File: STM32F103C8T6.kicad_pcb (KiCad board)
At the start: 2 copper layers, 39.4 x 64.8 mm, 51 parts, among them J1 USB_Device, J2 USB_TTL, P1 L-Pin, P2 R-Pin, P3 DEBUG, SW1 NRST, U1 MIC5219-3.3YM5, U2 CH340E, U3 STM32F103C8Tx, Y1 8MHz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

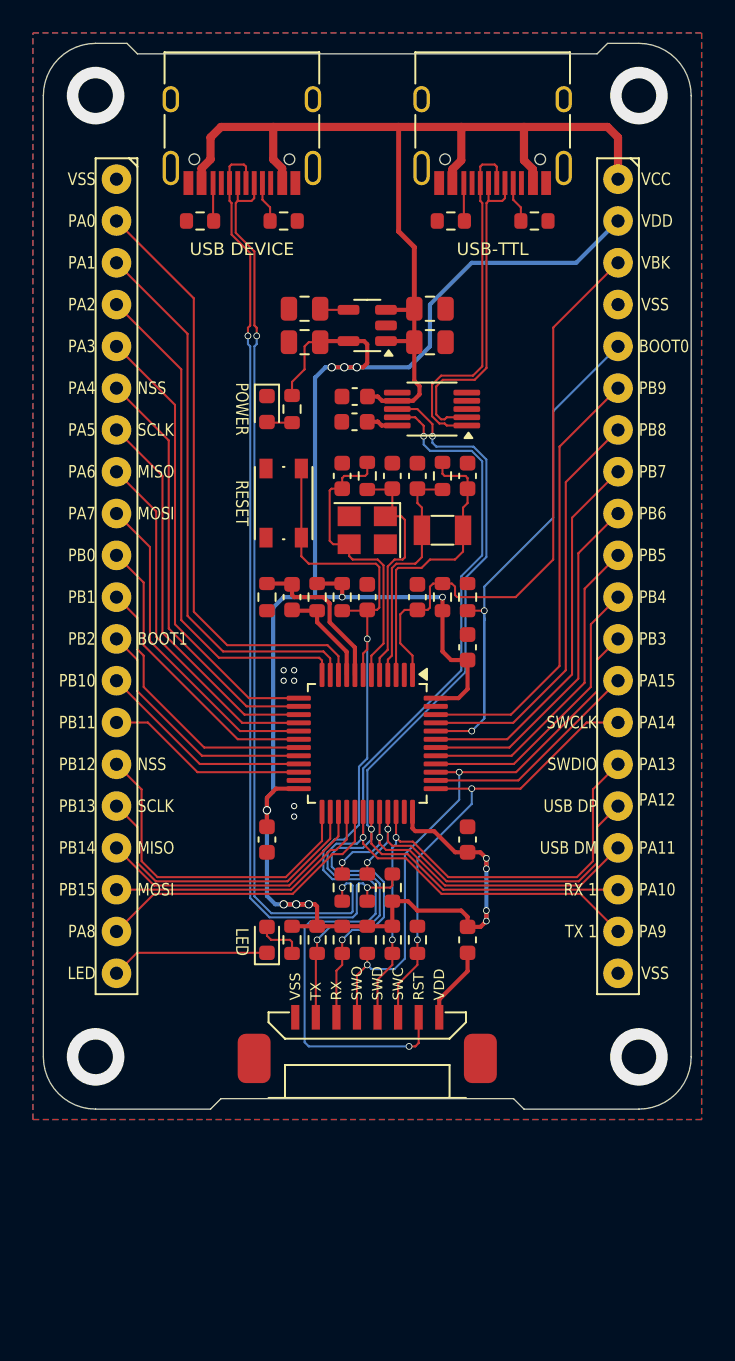
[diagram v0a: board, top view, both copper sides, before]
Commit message: 增加独立的电源连接端子
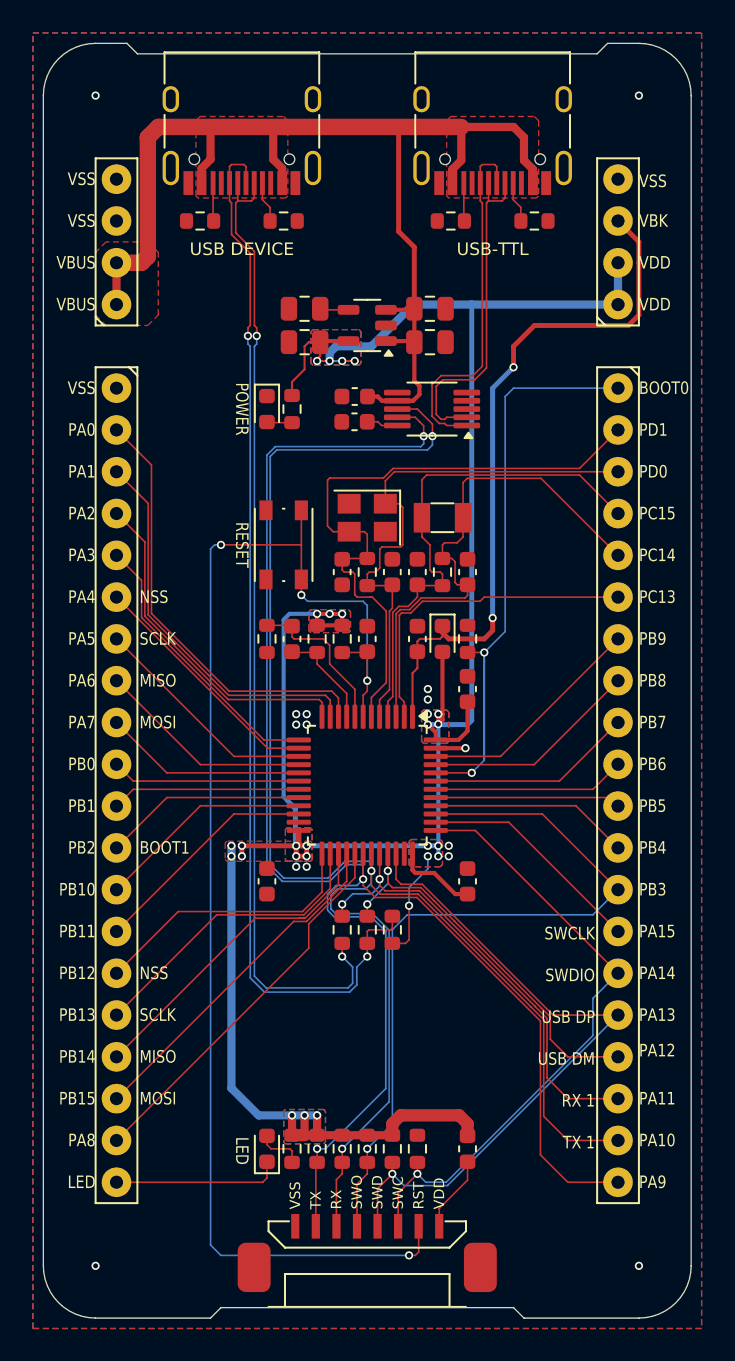
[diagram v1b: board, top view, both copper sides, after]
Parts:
- removed R15: 0R, Resistor_SMD:R_0603_1608Metric
- added D3: 1N4148, Diode_SMD:D_0603_1608Metric, F.Cu at (154.6, 115.6)
- added P4: POWER-R, Append_Connector:HDR1×4_2.54mm, F.Cu at (165.2, 95.2)
- added P5: POWER-L, Append_Connector:HDR1×4_2.54mm, F.Cu at (134.8, 95.2)
- moved D2 12.7 mm to (143.9, 146.5)
- moved F1 12.7 mm to (156.1, 146.5)
- moved P1 12.7 mm to (134.8, 100.3)
- moved P2 12.7 mm to (165.2, 100.3)
- moved P3 12.7 mm to (150.0, 151.8)
- moved R17 12.7 mm to (147.0, 146.5)
- moved R18 12.7 mm to (148.5, 146.5)
- moved R19 12.7 mm to (150.0, 146.5)
- moved R20 12.7 mm to (151.5, 146.5)
- moved R21 12.7 mm to (153.0, 146.5)
- moved R7 12.7 mm to (145.4, 146.5)
- moved C10 5.84 mm to (153.0, 111.5)
- moved C7 5.84 mm to (151.5, 111.5)
- moved C8 5.84 mm to (148.5, 111.5), turned to -90 degrees
- moved C9 5.84 mm to (156.1, 111.5)
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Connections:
- P2 pad 1: VBUS -> /BOOT0
- P2 pad 10: /PB5 -> /PB6
- P2 pad 11: /PB4 -> /PB5
- P2 pad 12: /PB3/SWO -> /PB4
- P2 pad 13: /PA15 -> /PB3/SWO
- P2 pad 14: /PA14/SWCLK -> /PA15
- P2 pad 15: /PA13/SWDIO -> /PA14/SWCLK
- P2 pad 16: /PA12/USBDP -> /PA13/SWDIO
- P2 pad 17: /PA11/USBDM -> /PA12/USBDP
- P2 pad 18: /PA10/USART_RX -> /PA11/USBDM
- P2 pad 19: /PA9/USART_TX -> /PA10/USART_RX
- P2 pad 2: VDD -> /PD1/OSC_OUT
- P2 pad 20: VSS -> /PA9/USART_TX
- P2 pad 3: VBAT -> /PD0/OSC_IN
- P2 pad 4: VSS -> /PC15/OSC32_OUT
- P2 pad 5: /BOOT0 -> /PC14/OSC32_IN
- P2 pad 6: /PB9 -> /PC13
- P2 pad 7: /PB8 -> /PB9
- P2 pad 8: /PB7 -> /PB8
- P2 pad 9: /PB6 -> /PB7
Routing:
- net VDD: track 124.8 -> 164.1 mm, vias 13 -> 27
- net /PA10/USART_RX: track 68.8 -> 100.7 mm
- net /PA9/USART_TX: track 70.6 -> 102.4 mm
- net VBUS: track 65.5 -> 87.5 mm
- net /NRST: track 60.3 -> 82.1 mm, vias 2 -> 4
- net /PD1/OSC_OUT: track 18.1 -> 39.2 mm
- net /PC13: track 0.00 -> 20.0 mm
- net /PD0/OSC_IN: track 15.0 -> 33.3 mm
- net /PC15/OSC32_OUT: track 14.5 -> 30.9 mm
- net /PC14/OSC32_IN: track 17.8 -> 31.7 mm
- net /PB9: track 27.1 -> 14.0 mm
- net /PB8: track 25.1 -> 13.2 mm
- net /PB3/SWO: track 35.0 -> 46.6 mm, vias 2 -> 1
- net /PA4: track 25.8 -> 14.9 mm
- net /PB7: track 23.4 -> 12.6 mm
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- added copper zone on F.Cu, net VBUS
- added copper zone on B.Cu, net VDD
- added copper zone on F.Cu, net VDD
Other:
- board size 39.4 x 64.8 mm -> 39.4 x 77.5 mm
- board text added: "PC13"
- board text added: "PC14"
- board text added: "PC15"
- board text added: "PD0"
- board text added: "PD1"
- board text added: "VBUS"
- board text removed: "VCC"

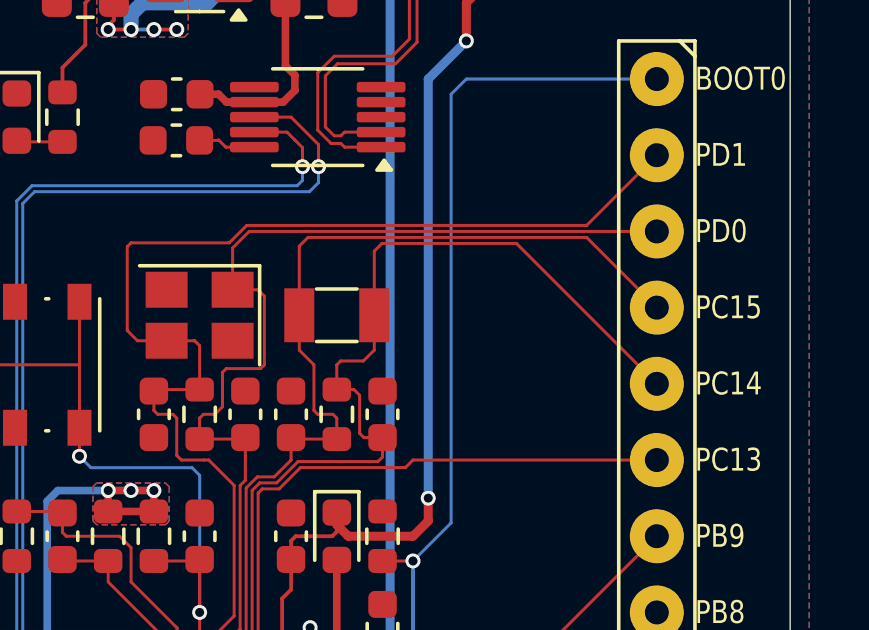
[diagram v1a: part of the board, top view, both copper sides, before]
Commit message: 修正晶振匹配电容铺地连接错误的问题
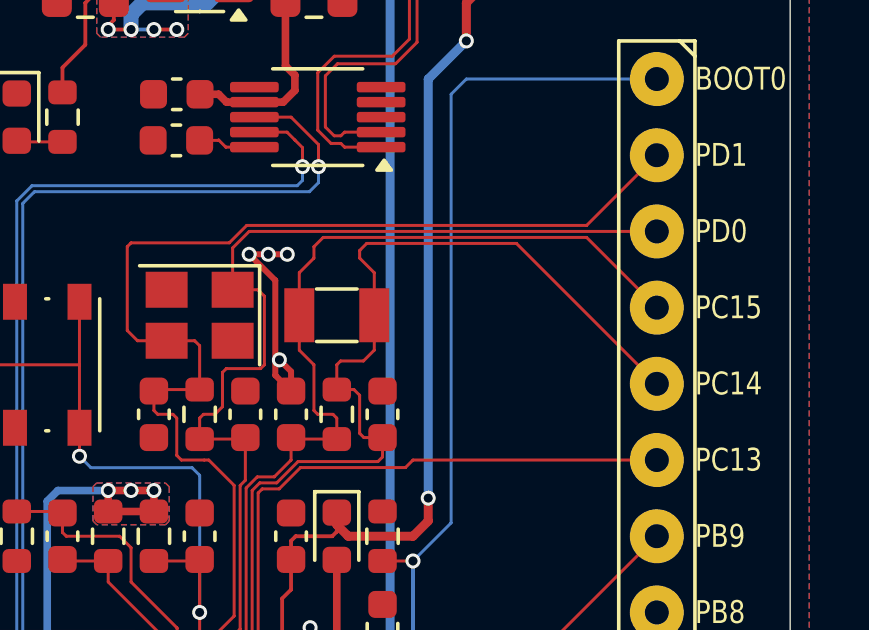
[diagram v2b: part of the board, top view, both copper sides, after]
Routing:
- net VSS: track 1.81 -> 9.42 mm, vias 11 -> 15
- net /PC14/OSC32_IN: track 31.7 -> 32.4 mm
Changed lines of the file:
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@@
 		)
 		(property "Value" "22pF"
-			(at -0.1524 0 360)
+			(at -0.1524 0 0)
 			(layer "F.Fab")
 			(effects
@@
 	)
 	(segment
+		(start 152.522 107.033)
+		(end 151.651 106.162)
+		(width 0.2)
+		(layer "F.Cu")
+		(net 1)
+	)
+	(segment
+		(start 153.048 110.721)
+		(end 153.048 110.068883)
+		(width 0.2)
+		(layer "F.Cu")
+		(net 1)
+	)
+	(segment
+		(start 153.048 110.721)
+		(end 152.522 110.195)
+		(width 0.2)
+		(layer "F.Cu")
+		(net 1)
+	)
+	(segment
+		(start 151.651 106.162)
+		(end 152.286 106.162)
+		(width 0.2)
+		(layer "F.Cu")
+		(net 1)
+	)
+	(segment
+		(start 153.048 110.068883)
+		(end 152.659 109.679883)
+		(width 0.2)
+		(layer "F.Cu")
+		(net 1)
+	)
+	(segment
 		(start 154.1625 122.2)
 		(end 155.969 122.2)
@@
 		(net 1)
 	)
+	(segment
+		(start 152.286 106.162)
+		(end 152.921 106.162)
+		(width 0.2)
+		(layer "F.Cu")
+		(net 1)
+	)
+	(segment
+		(start 152.522 110.195)
+		(end 152.522 107.033)
+		(width 0.2)
+		(layer "F.Cu")
+		(net 1)
+	)
+	(via
+		(at 151.651 106.162)
+		(size 0.5)
+		(drill 0.3)
+		(layers "F.Cu" "B.Cu")
+		(net 1)
+	)
 	(via
 		(at 153.683 119.243)
@@
 	)
 	(via
+		(at 152.659 109.679883)
+		(size 0.5)
+		(drill 0.3)
+		(layers "F.Cu" "B.Cu")
+		(net 1)
+	)
+	(via
+		(at 152.286 106.162)
+		(size 0.5)
+		(drill 0.3)
+		(layers "F.Cu" "B.Cu")
+		(net 1)
+	)
+	(via
+		(at 152.921 106.162)
+		(size 0.5)
+		(drill 0.3)
+		(layers "F.Cu" "B.Cu")
+		(net 1)
+	)
+	(via
 		(at 154.953 128.133)
 		(size 0.5)
@@
 	)
 	(segment
-		(start 153.280042 113.0708)
-		(end 155.9436 113.0708)
+		(start 155.822 106.777)
+		(end 155.822 108.194)
 		(width 0.1)
 		(layer "F.Cu")
@@
 	)
 	(segment
-		(start 155.822 106.055)
-		(end 155.822 108.194)
+		(start 153.280042 113.0708)
+		(end 155.9436 113.0708)
 		(width 0.1)
 		(layer "F.Cu")
@@
 	)
 	(segment
-		(start 160.56 105.8)
-		(end 156.077 105.8)
-		(width 0.1)
-		(layer "F.Cu")
-		(net 7)
-	)
-	(segment
-		(start 165.24 110.48)
-		(end 160.56 105.8)
-		(width 0.1)
-		(layer "F.Cu")
-		(net 7)
-	)
-	(segment
 		(start 155.474 112.271)
 		(end 155.334 112.131)
@@
 	)
 	(segment
+		(start 155.334 106.289)
+		(end 155.822 106.777)
+		(width 0.1)
+		(layer "F.Cu")
+		(net 7)
+	)
+	(segment
 		(start 156.096 112.271)
 		(end 155.474 112.271)
@@
 	)
 	(segment
+		(start 155.569 105.8)
+		(end 155.334 106.035)
+		(width 0.1)
+		(layer "F.Cu")
+		(net 7)
+	)
+	(segment
 		(start 152.568842 113.782)
 		(end 153.280042 113.0708)
@@
 	)
 	(segment
+		(start 165.24 110.48)
+		(end 160.56 105.8)
+		(width 0.1)
+		(layer "F.Cu")
+		(net 7)
+	)
+	(segment
+		(start 160.56 105.8)
+		(end 155.569 105.8)
+		(width 0.1)
+		(layer "F.Cu")
+		(net 7)
+	)
+	(segment
 		(start 154.572 109.845)
 		(end 154.572 110.671)
@@
 	)
 	(segment
-		(start 156.077 105.8)
-		(end 155.822 106.055)
+		(start 155.334 106.035)
+		(end 155.334 106.289)
 		(width 0.1)
 		(layer "F.Cu")
@@
 	)
 	(segment
-		(start 153.322 105.888)
-		(end 153.61 105.6)
-		(width 0.1)
-		(layer "F.Cu")
-		(net 8)
-	)
-	(segment
 		(start 153.322 108.194)
 		(end 153.322 109.357)
@@
 	)
 	(segment
+		(start 162.9 105.6)
+		(end 154.118 105.6)
+		(width 0.1)
+		(layer "F.Cu")
+		(net 8)
+	)
+	(segment
 		(start 153.937 111.496)
 		(end 154.445 111.496)
@@
 	)
 	(segment
+		(start 153.81 105.908)
+		(end 153.81 106.289)
+		(width 0.1)
+		(layer "F.Cu")
+		(net 8)
+	)
+	(segment
 		(start 153.098 112.321)
 		(end 153.048 112.271)
@@
 	)
 	(segment
-		(start 153.322 108.194)
-		(end 153.322 105.888)
-		(width 0.1)
-		(layer "F.Cu")
-		(net 8)
-	)
-	(segment
 		(start 153.322 109.357)
 		(end 153.81 109.845)
@@
 	)
 	(segment
-		(start 151.920315 113.582)
-		(end 152.486 113.582)
+		(start 153.322 106.777)
+		(end 153.322 108.194)
 		(width 0.1)
 		(layer "F.Cu")
@@
 	)
 	(segment
-		(start 162.9 105.6)
-		(end 165.24 107.94)
+		(start 151.920315 113.582)
+		(end 152.486 113.582)
 		(width 0.1)
 		(layer "F.Cu")
@@
 	)
 	(segment
-		(start 151.55 119.062)
-		(end 151.55 113.952315)
+		(start 154.118 105.6)
+		(end 153.81 105.908)
+		(width 0.1)
+		(layer "F.Cu")
+		(net 8)
+	)
+	(segment
+		(start 153.81 106.289)
+		(end 153.322 106.777)
 		(width 0.1)
 		(layer "F.Cu")
@@
 	)
 	(segment
-		(start 153.61 105.6)
+		(start 165.24 107.94)
 		(end 162.9 105.6)
 		(width 0.1)
 		(layer "F.Cu")
+		(net 8)
+	)
+	(segment
+		(start 151.55 119.062)
+		(end 151.55 113.952315)
+		(width 0.1)
+		(layer "F.Cu")

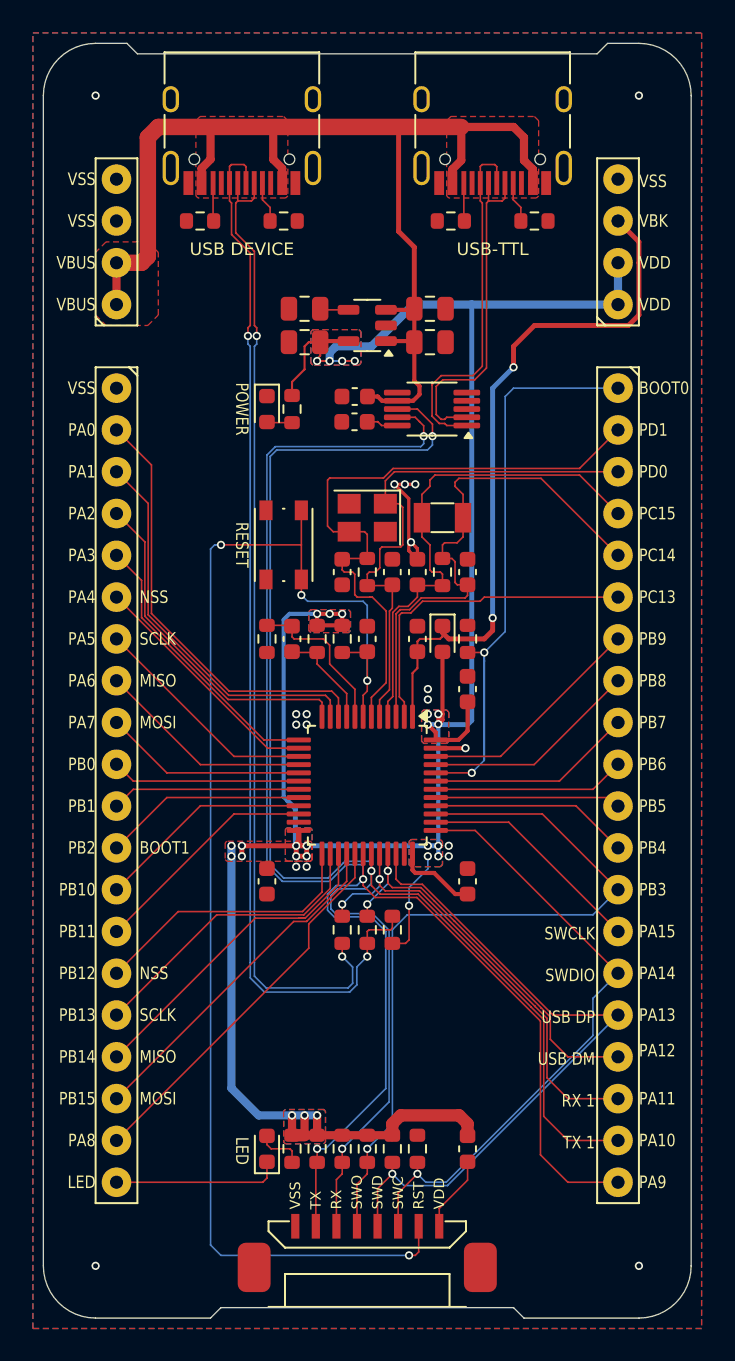
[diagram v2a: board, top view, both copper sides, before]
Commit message: 修正电器规则和布线错误
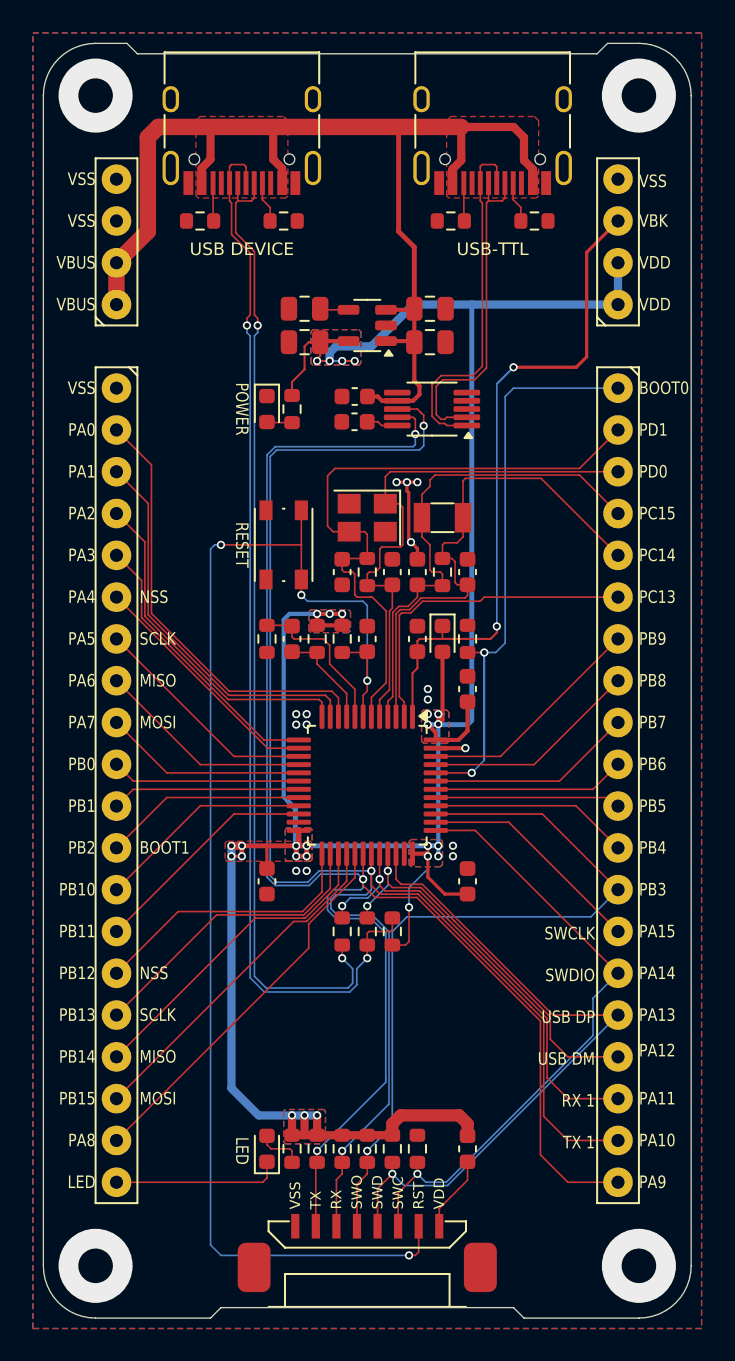
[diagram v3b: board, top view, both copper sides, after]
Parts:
- moved R3 0.10 mm to (151.5, 133.3)
- moved R4 0.10 mm to (148.5, 133.3)
- moved R5 0.10 mm to (150.0, 133.3)
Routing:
- net VDD: track 164.1 -> 167.6 mm
- net VBAT: track 43.3 -> 40.8 mm
- net VSS: track 9.42 -> 8.03 mm
- net /PA9/USART_TX: track 102.4 -> 101.3 mm
- net VBUS: track 87.5 -> 86.6 mm
- net /PC14/OSC32_IN: track 32.4 -> 31.7 mm
- net /PA10/USART_RX: track 100.7 -> 100.1 mm

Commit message: 更新电路设计，兼容F401CC芯片
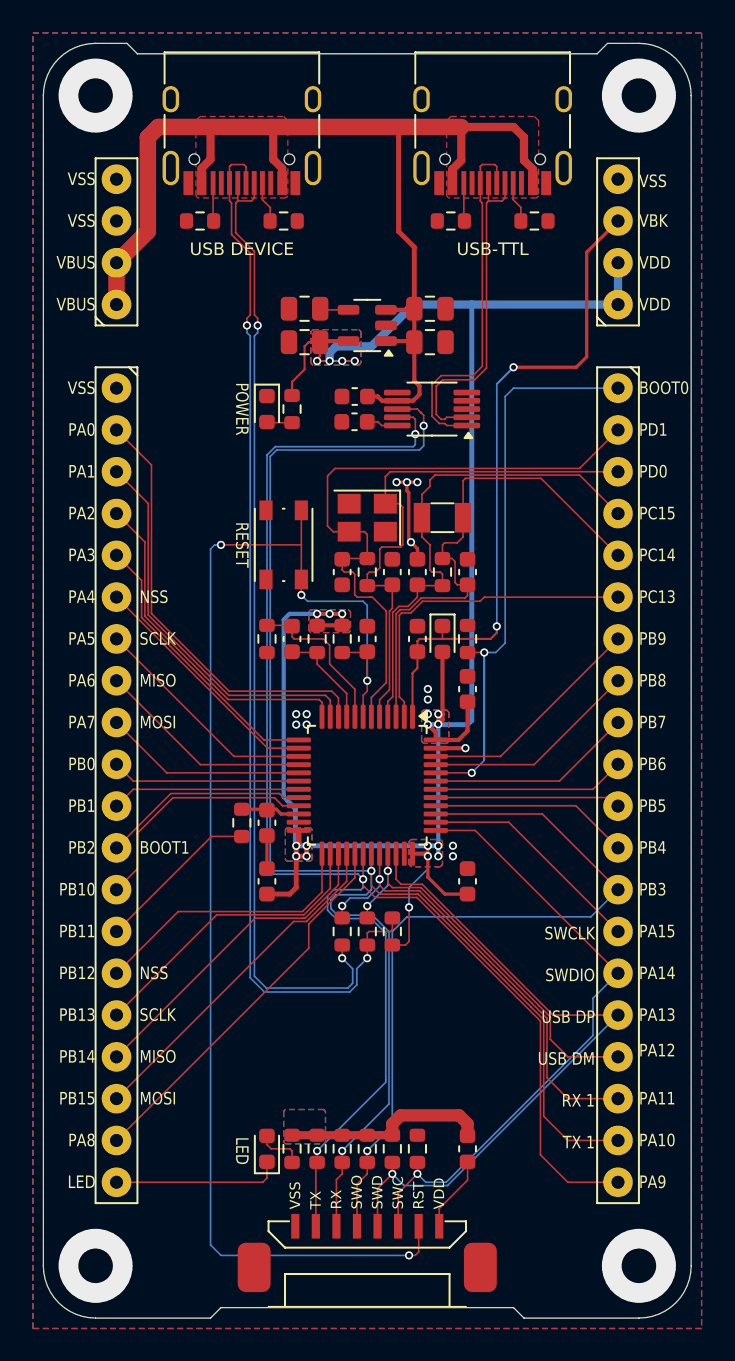
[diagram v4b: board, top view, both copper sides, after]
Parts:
- added C17: 2.2uF, Capacitor_SMD:C_0603_1608Metric, F.Cu at (143.9, 126.7)
- added R15: 0R, Resistor_SMD:R_0603_1608Metric, F.Cu at (142.4, 126.7)
- U3: value STM32F103C8Tx -> F103C8_Class
- turned C13 to 90 degrees
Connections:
- C15 pad 1: VDD -> VSS
- U3 pad 22: /PB11 -> /VCAP
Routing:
- net VDD: track 167.6 -> 140.0 mm, vias 27 -> 20
- net /PB11: track 14.0 -> 10.0 mm
- net /VCAP: track 0.00 -> 3.58 mm
- net VSS: track 8.03 -> 10.0 mm, vias 15 -> 13
- net /PB10: track 13.2 -> 14.9 mm
- net /PA10/USART_RX: track 100.1 -> 99.3 mm
- net /PA9/USART_TX: track 101.3 -> 100.5 mm
